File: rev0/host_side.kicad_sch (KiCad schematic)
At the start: 21 parts, among them IC1 ECP5-BGA256, U11 USB3343-CP

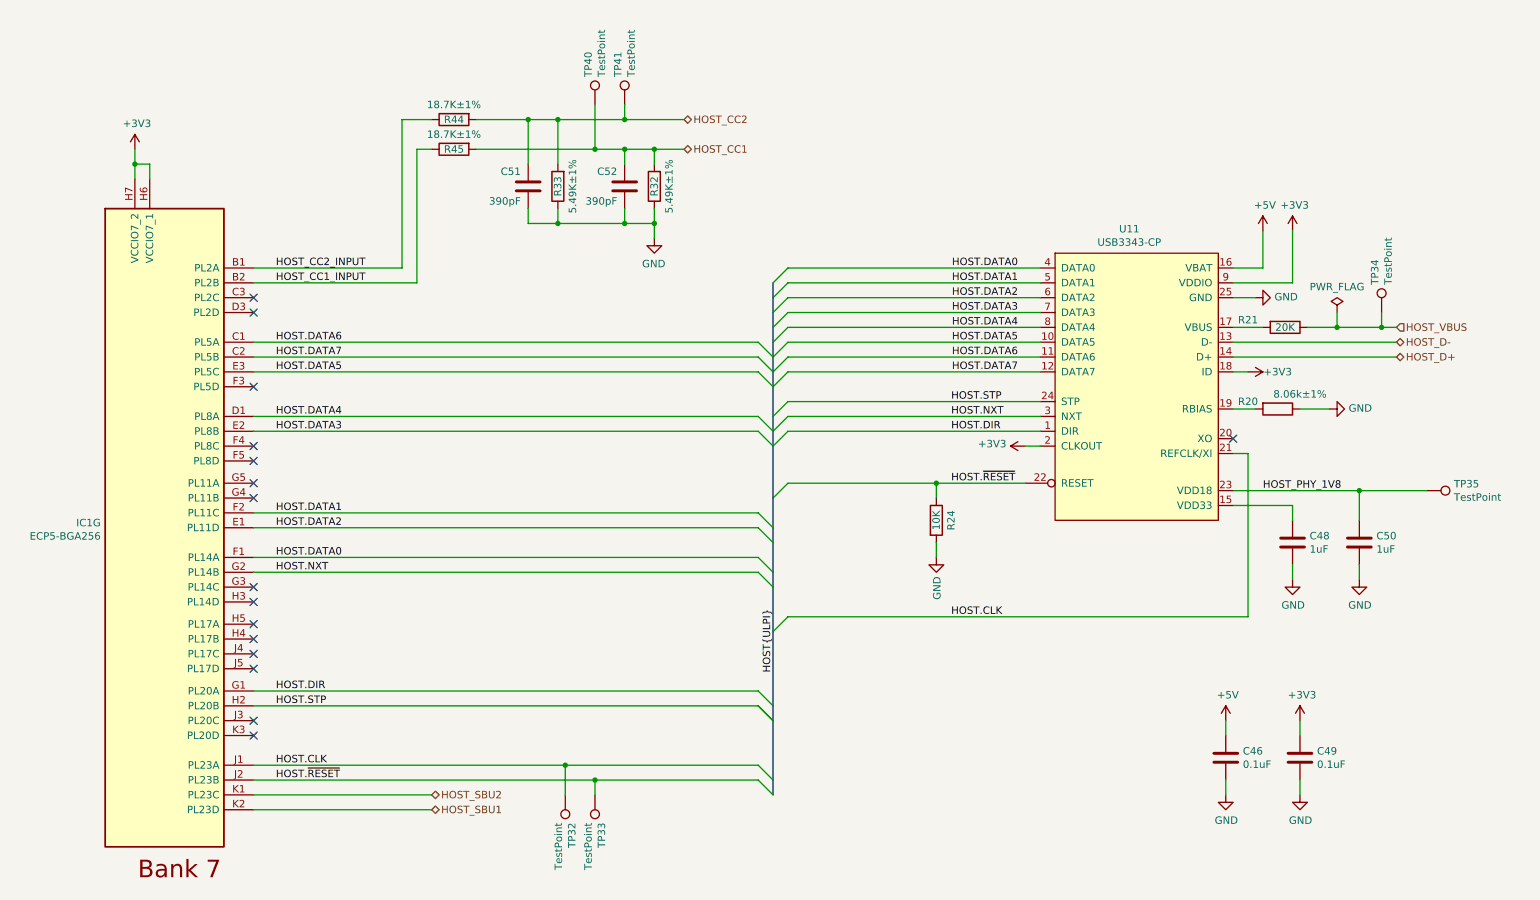
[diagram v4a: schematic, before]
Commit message: hardware: consistently use lowercase k for kilo
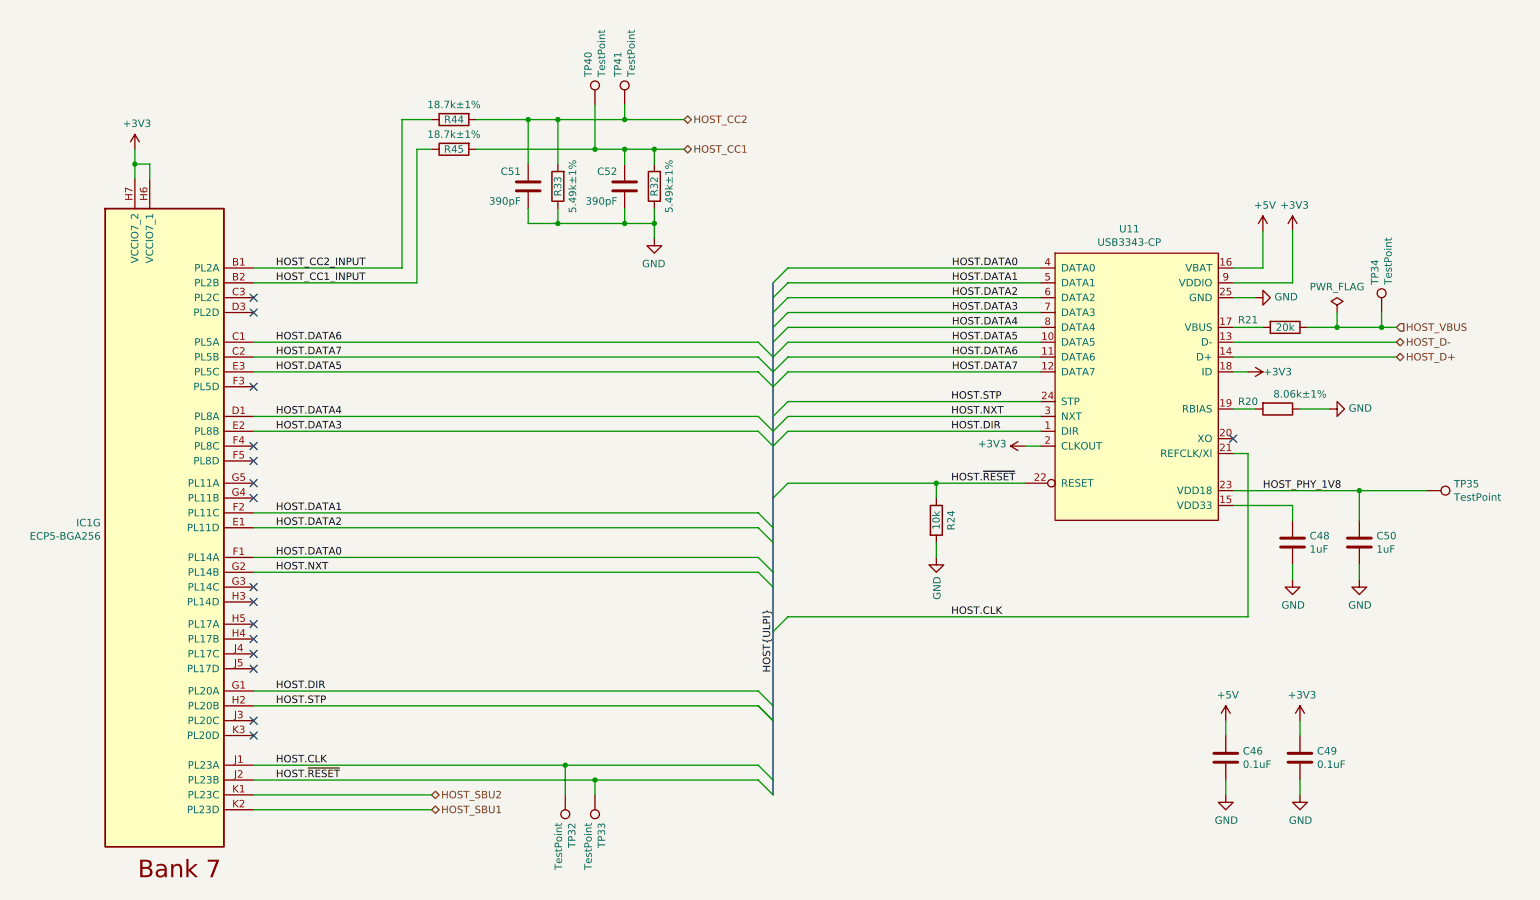
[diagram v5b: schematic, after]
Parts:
- R21: value 20K -> 20k
- R24: value 10K -> 10k
- R32, R33: value 5.49K±1% -> 5.49k±1%
- R44, R45: value 18.7K±1% -> 18.7k±1%
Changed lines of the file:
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@@
     (in_bom yes) (on_board yes)
     (property "Reference" "R21" (id 0) (at 229.87 67.31 90))
-    (property "Value" "20K" (id 1) (at 236.22 68.58 90))
+    (property "Value" "20k" (id 1) (at 236.22 68.58 90))
     (property "Footprint" "Resistor_SMD:R_0402_1005Metric" (id 2) (at 236.22 66.802 90)
       (effects (font (size 1.27 1.27)) hide)
@@
     (in_bom yes) (on_board yes)
     (property "Reference" "R24" (id 0) (at 179.07 101.6 90))
-    (property "Value" "10K" (id 1) (at 176.53 101.6 90))
+    (property "Value" "10k" (id 1) (at 176.53 101.6 90))
     (property "Footprint" "Resistor_SMD:R_0402_1005Metric" (id 2) (at 174.752 101.6 90)
       (effects (font (size 1.27 1.27)) hide)
@@
     (in_bom yes) (on_board yes)
     (property "Reference" "R44" (id 0) (at 93.98 33.02 90))
-    (property "Value" "18.7K±1%" (id 1) (at 93.98 30.48 90))
+    (property "Value" "18.7k±1%" (id 1) (at 93.98 30.48 90))
     (property "Footprint" "Resistor_SMD:R_0402_1005Metric" (id 2) (at 93.98 31.242 90)
       (effects (font (size 1.27 1.27)) hide)
@@
     (in_bom yes) (on_board yes)
     (property "Reference" "R45" (id 0) (at 93.98 38.1 90))
-    (property "Value" "18.7K±1%" (id 1) (at 93.98 35.56 90))
+    (property "Value" "18.7k±1%" (id 1) (at 93.98 35.56 90))
     (property "Footprint" "Resistor_SMD:R_0402_1005Metric" (id 2) (at 93.98 36.322 90)
       (effects (font (size 1.27 1.27)) hide)
@@
     (in_bom yes) (on_board yes)
     (property "Reference" "R32" (id 0) (at 128.27 44.45 90))
-    (property "Value" "5.49K±1%" (id 1) (at 130.81 44.45 90))
+    (property "Value" "5.49k±1%" (id 1) (at 130.81 44.45 90))
     (property "Footprint" "Resistor_SMD:R_0402_1005Metric" (id 2) (at 130.048 44.45 90)
       (effects (font (size 1.27 1.27)) hide)
@@
     (in_bom yes) (on_board yes)
     (property "Reference" "R33" (id 0) (at 111.76 44.45 90))
-    (property "Value" "5.49K±1%" (id 1) (at 114.3 44.45 90))
+    (property "Value" "5.49k±1%" (id 1) (at 114.3 44.45 90))
     (property "Footprint" "Resistor_SMD:R_0402_1005Metric" (id 2) (at 113.538 44.45 90)
       (effects (font (size 1.27 1.27)) hide)

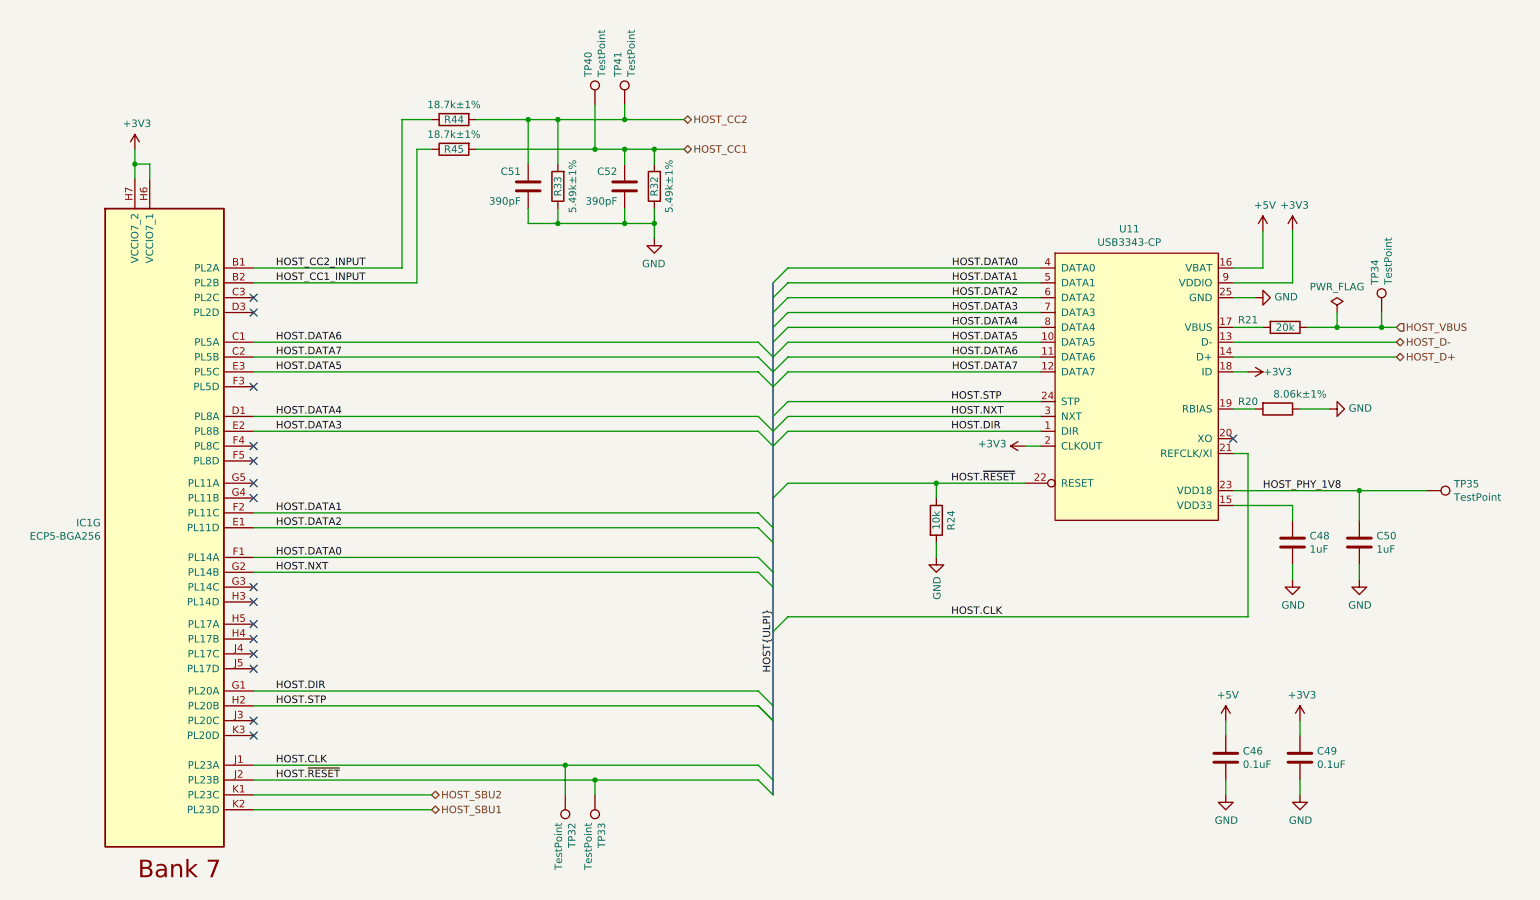
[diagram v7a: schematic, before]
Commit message: hardware: reassign FPGA I/O banks
assign HyperRAM to DQS group
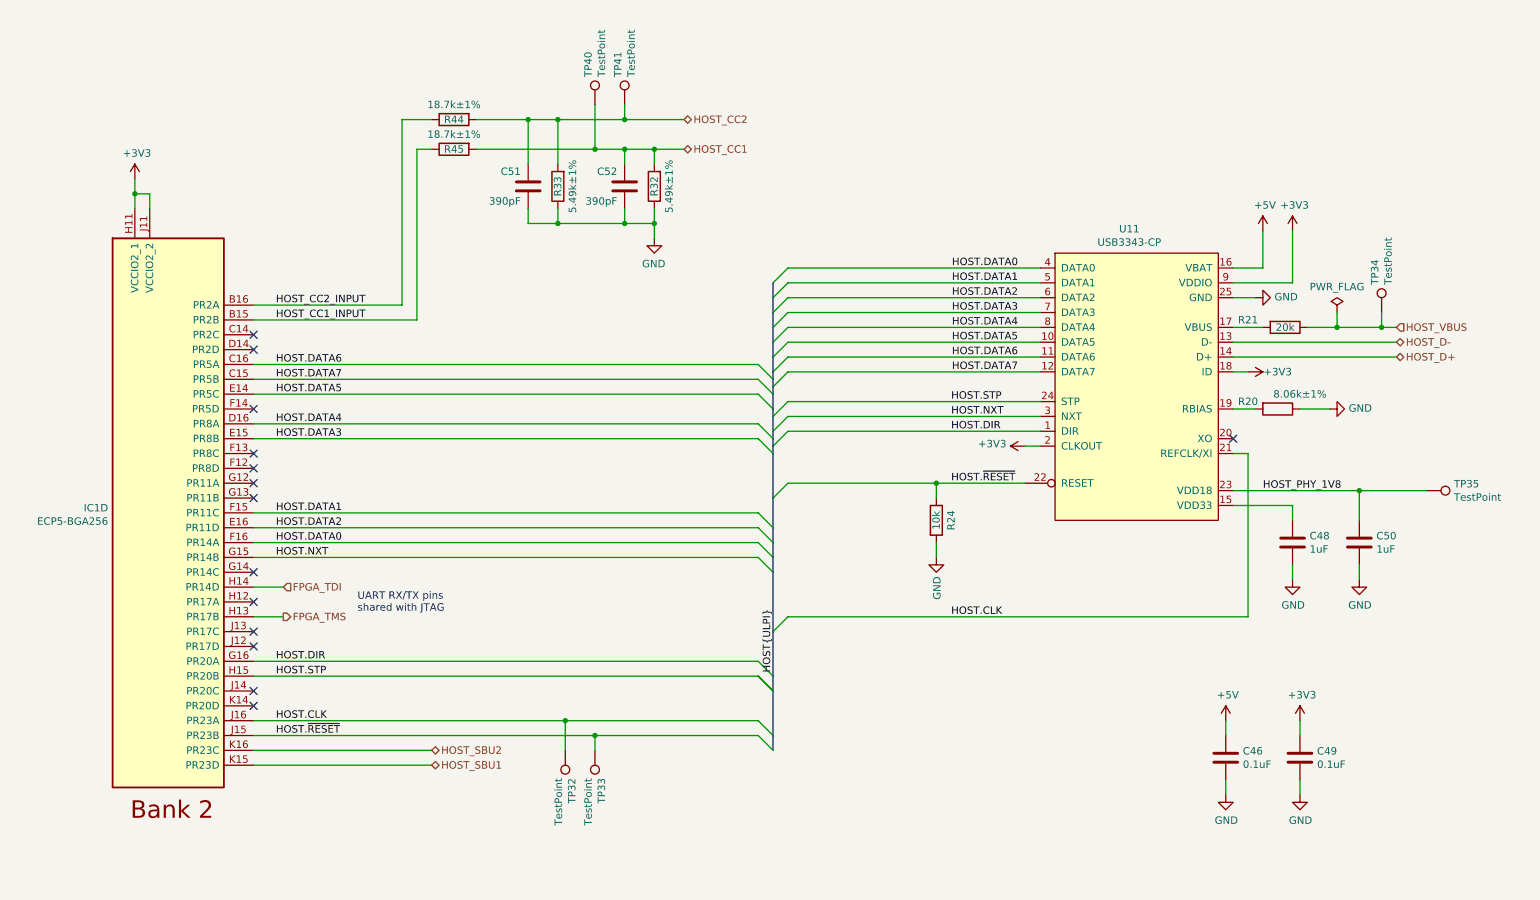
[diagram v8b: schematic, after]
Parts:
- removed IC1: ECP5-BGA256, luna:lattice_cabga256, symbol fpgas_and_processors:ECP5-BGA256
- added IC1: ECP5-BGA256, luna:lattice_cabga256, symbol fpgas_and_processors:ECP5-BGA256
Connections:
- net +3V3: now also IC1.H11 (VCCIO2_1), IC1.J11 (VCCIO2_2)
- net HOST.CLK: now also IC1.J16 (PR23A)
- net HOST.DATA0: now also IC1.F16 (PR14A)
- net HOST.DATA1: now also IC1.F15 (PR11C)
- net HOST.DATA2: now also IC1.E16 (PR11D)
- net HOST.DATA3: now also IC1.E15 (PR8B)
- net HOST.DATA4: now also IC1.D16 (PR8A)
- net HOST.DATA5: now also IC1.E14 (PR5C)
- net HOST.DATA6: now also IC1.C16 (PR5A)
- net HOST.DATA7: now also IC1.C15 (PR5B)
- net HOST.DIR: now also IC1.G16 (PR20A)
- net HOST.NXT: now also IC1.G15 (PR14B)
- net HOST.STP: now also IC1.H15 (PR20B)
- net HOST.~{RESET}: now also IC1.J15 (PR23B)
- net HOST_CC1_INPUT: now also IC1.B15 (PR2B)
- net HOST_CC2_INPUT: now also IC1.B16 (PR2A)
- net HOST_SBU1: now also IC1.K15 (PR23D)
- net HOST_SBU2: now also IC1.K16 (PR23C)
- new net FPGA_TDI: IC1.H14 (PR14D)
- new net FPGA_TMS: IC1.H13 (PR17B)
- no-connect marks 16 -> 14
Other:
- note added: "UART RX/TX pins shared with JTAG"
- moved on the sheet: TP32, TP33
